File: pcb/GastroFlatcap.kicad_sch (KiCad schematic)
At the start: 8 parts, among them J1 INPUT 12V, J2 LED, J3 SERVO, Q1 IRLZ44N

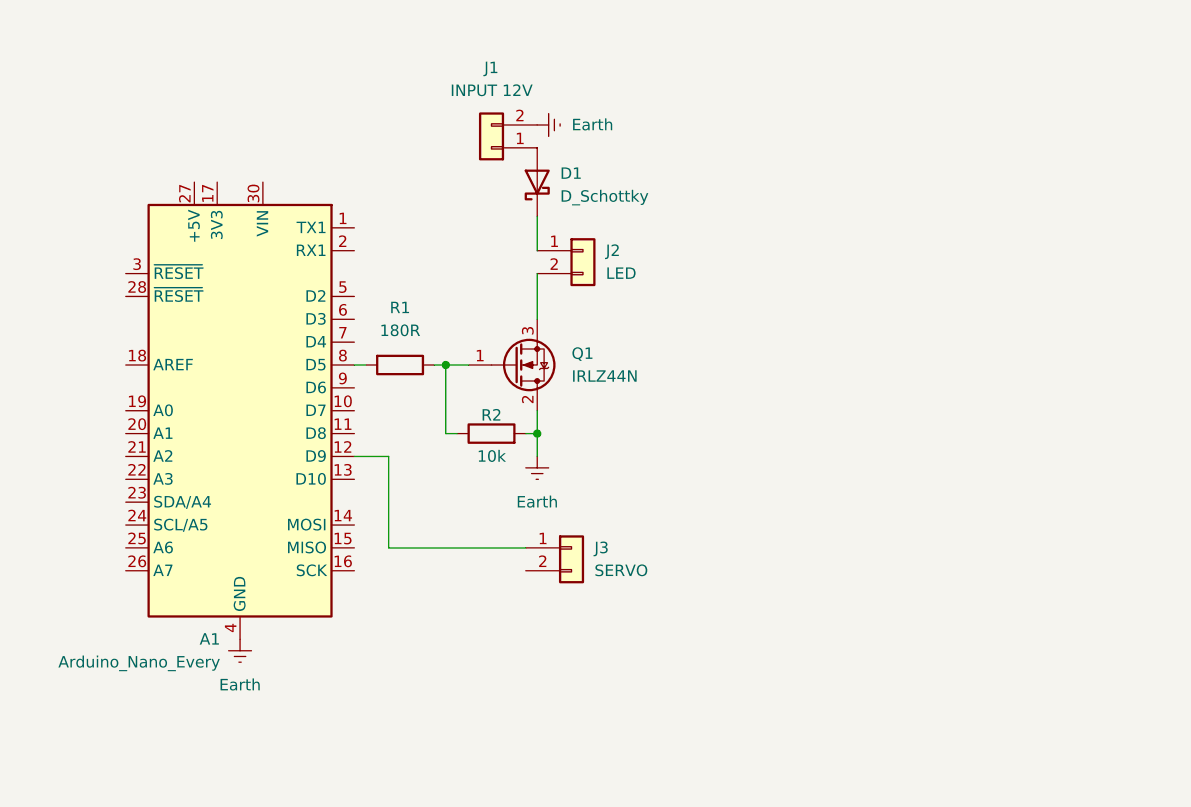
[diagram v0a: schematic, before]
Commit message: Changed microcontroller to ESP32 S3, merged flatcap with focuser
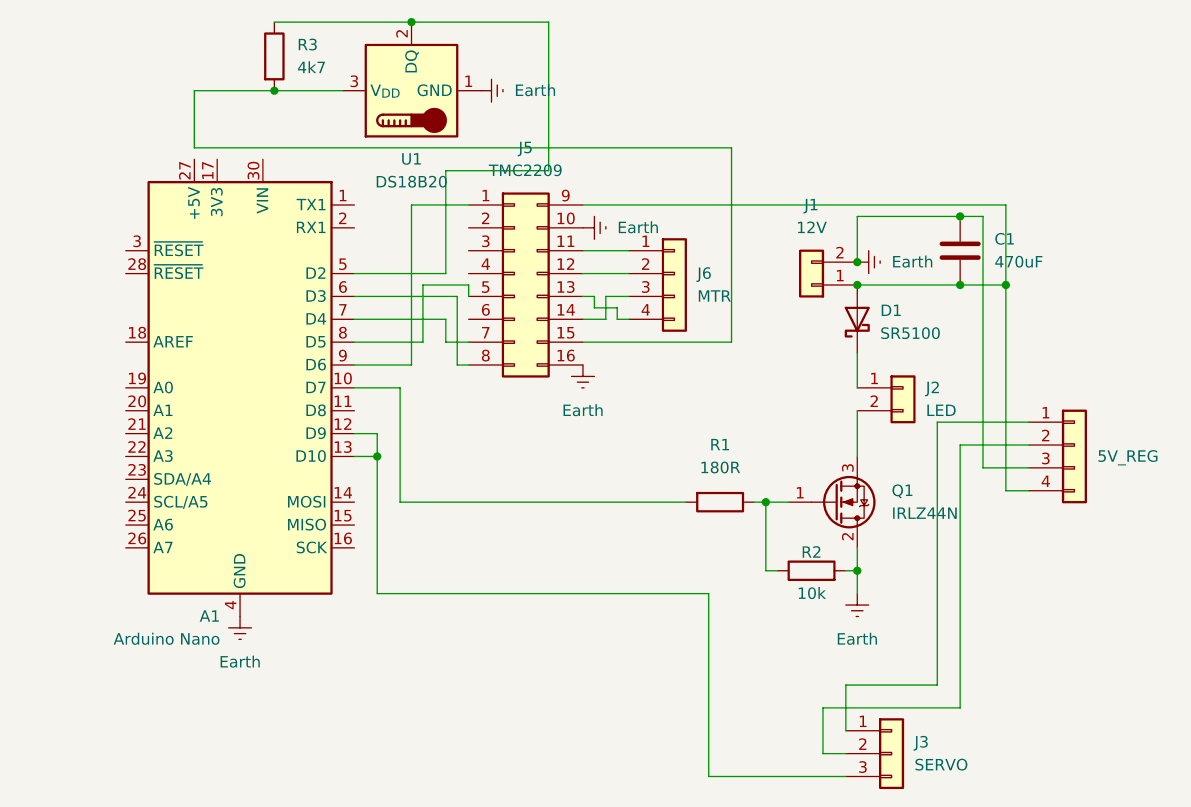
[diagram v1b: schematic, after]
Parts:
- removed J3: SERVO, Connector_JST:JST_XH_B2B-XH-A_1x02_P2.50mm_Vertical, symbol Connector_Generic:Conn_01x02
- added C1: 470uF, Capacitor_THT:CP_Radial_D6.3mm_P2.50mm, symbol Device:C
- added J3: SERVO, Connector_JST:JST_XH_B3B-XH-A_1x03_P2.50mm_Vertical, symbol Connector_Generic:Conn_01x03
- added J4: 5V_REG, Custom:PinHeader_1x04_P6.00mm_Vertical, symbol Connector_Generic:Conn_01x04
- added J5: TMC2209, Custom:Pin_Header_02x08_6_spaces_2,50mm, symbol Connector_Generic:Conn_02x08_Top_Bottom
- added J6: MTR, Connector_JST:JST_XH_B4B-XH-A_1x04_P2.50mm_Vertical, symbol Connector_Generic:Conn_01x04
- added R3: 4k7, Resistor_THT:R_Axial_DIN0411_L9.9mm_D3.6mm_P12.70mm_Horizontal, symbol Device:R
- added U1: DS18B20, Connector_PinHeader_2.54mm:PinHeader_1x03_P2.54mm_Vertical, symbol Sensor_Temperature:DS18B20
- A1: value Arduino_Nano_Every -> Arduino Nano
- D1: value D_Schottky -> SR5100; footprint Diode_SMD:D_MELF-RM10_Universal_Handsoldering -> Diode_THT:D_DO-27_P15.24mm_Horizontal
- J1: value INPUT 12V -> 12V; footprint Connector_JST:JST_XH_B2B-XH-A_1x02_P2.50mm_Vertical -> Connector_BarrelJack:BarrelJack_CUI_PJ-063AH_Horizontal
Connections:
- net Earth: now also C1.1, J4.3 (Pin_3), J5.10 (Pin_10), J5.16 (Pin_16), U1.1 (GND)
- net at D1.2 (A), J1.1 (Pin_1): now also C1.2, J4.4 (Pin_4), J5.9 (Pin_9)
- net at A1.8 (D5): now also J5.5 (Pin_5); no longer R1.2
- net at A1.12 (D9): now also A1.13 (D10), J3.3 (Pin_3)
- net at A1.10 (D7): now also R1.2
- net at A1.5 (D2): now also R3.1, U1.2 (DQ)
- net at A1.6 (D3): now also J5.8 (Pin_8)
- net at A1.7 (D4): now also J5.7 (Pin_7)
- net at A1.9 (D6): now also J5.1 (Pin_1)
- new net: J5.11 (Pin_11), J6.1 (Pin_1)
- new net: J5.12 (Pin_12), J6.2 (Pin_2)
- new net: J5.13 (Pin_13), J6.4 (Pin_4)
- new net: J5.14 (Pin_14), J6.3 (Pin_3)
- new net: J5.15 (Pin_15), R3.2, U1.3 (V_{DD})
- new net: J3.1 (Pin_1), J4.1 (Pin_1)
- new net: J3.2 (Pin_2), J4.2 (Pin_2)
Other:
- moved on the sheet: A1, D1, J1, J2, Q1, R1, R2
